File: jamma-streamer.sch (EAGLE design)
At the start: 73 parts, among them IC1 LM7805, J1 Audio line out, J2 ICSP, J3 796136-1, J4 DM3AT-SF-PEJM5, J6 292304-1, T1 TY-145P, T2 TY-145P, U1 CD74HC165MD16-M, U10 LM358DTD8-M, U2 ATMEGA328PB-AUR, U3 74HC4050D, U4 TLV757X / LP298X, U5 CD74HC165MD16-M, U6 CD74HC165MD16-M, U7 FT232RL, U8 DS3231SNT&R21-0042B_16-M, U9 NDT2955SOT-223-M, Y1 16MHz

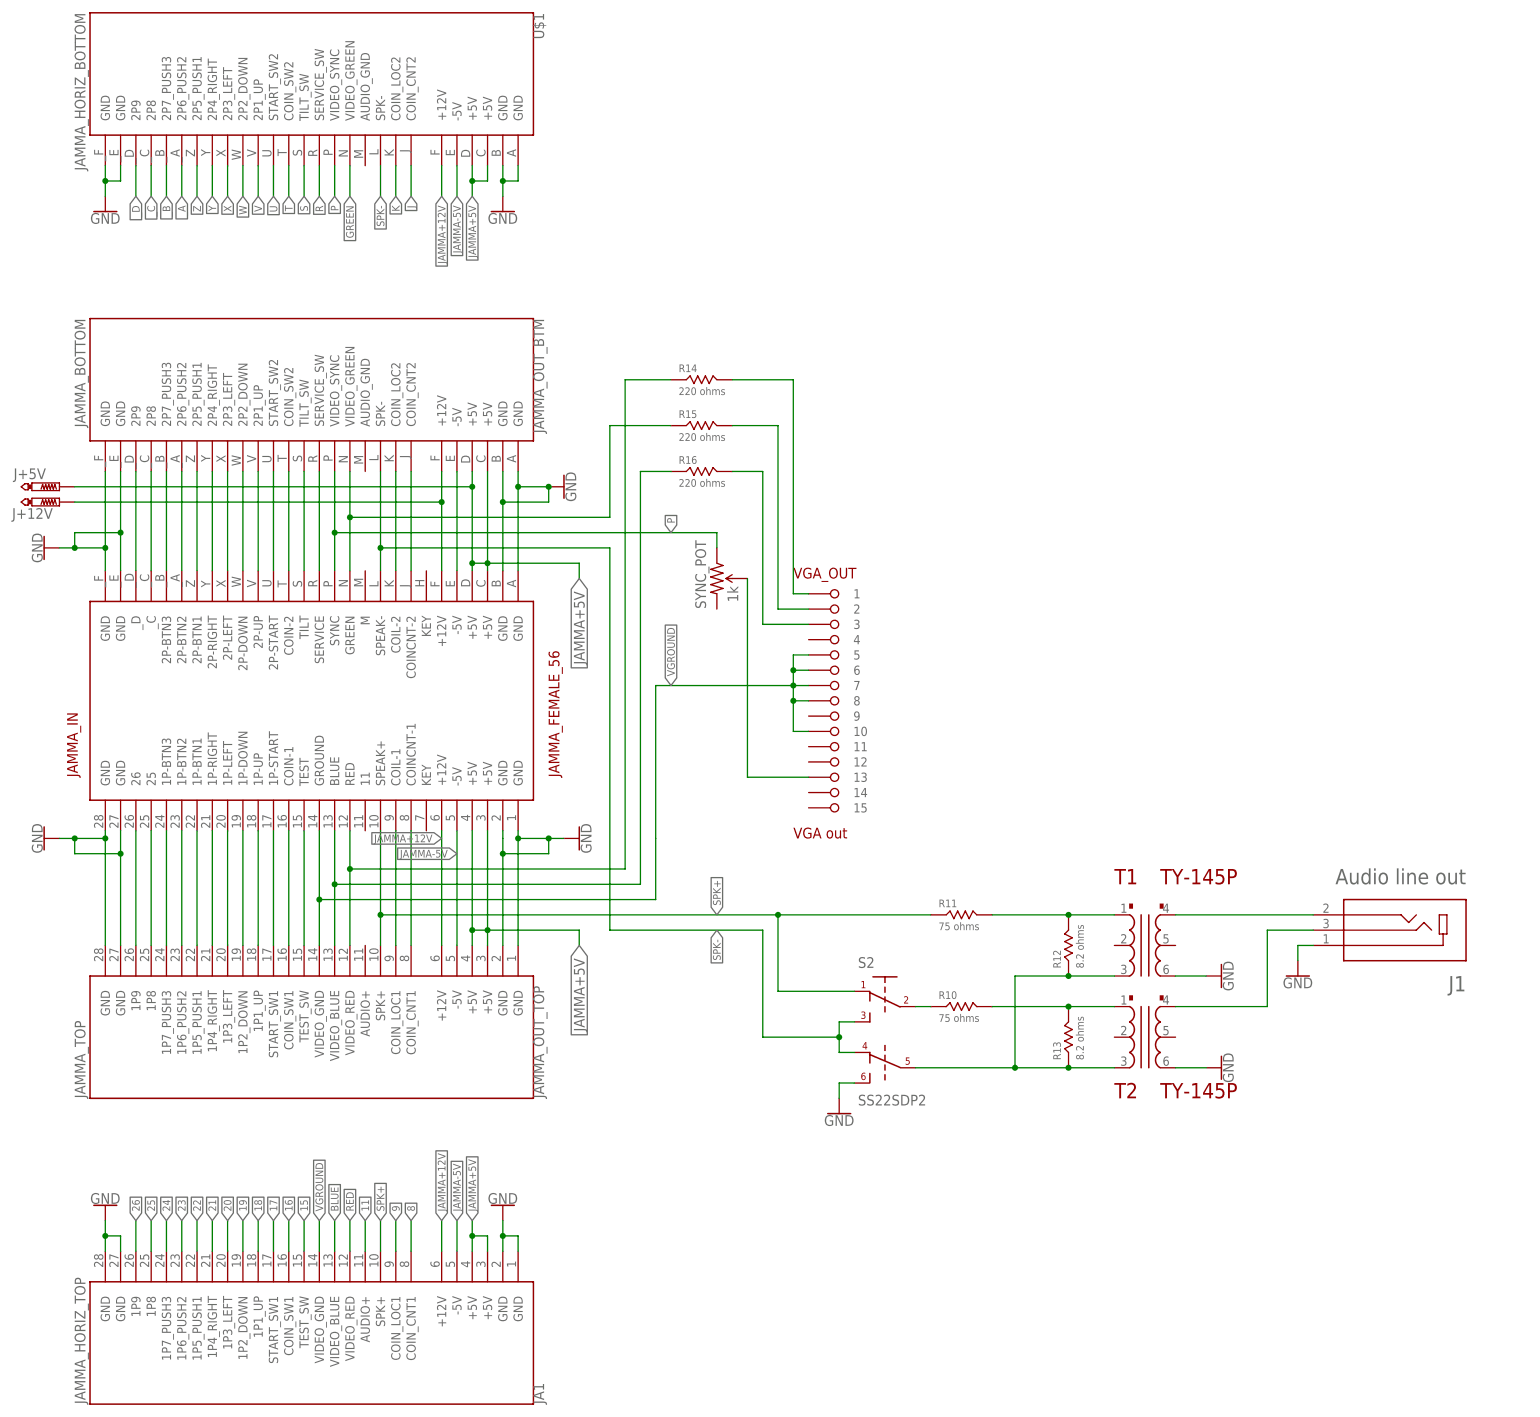
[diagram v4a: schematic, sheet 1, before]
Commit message: DRC Sparkfun ok
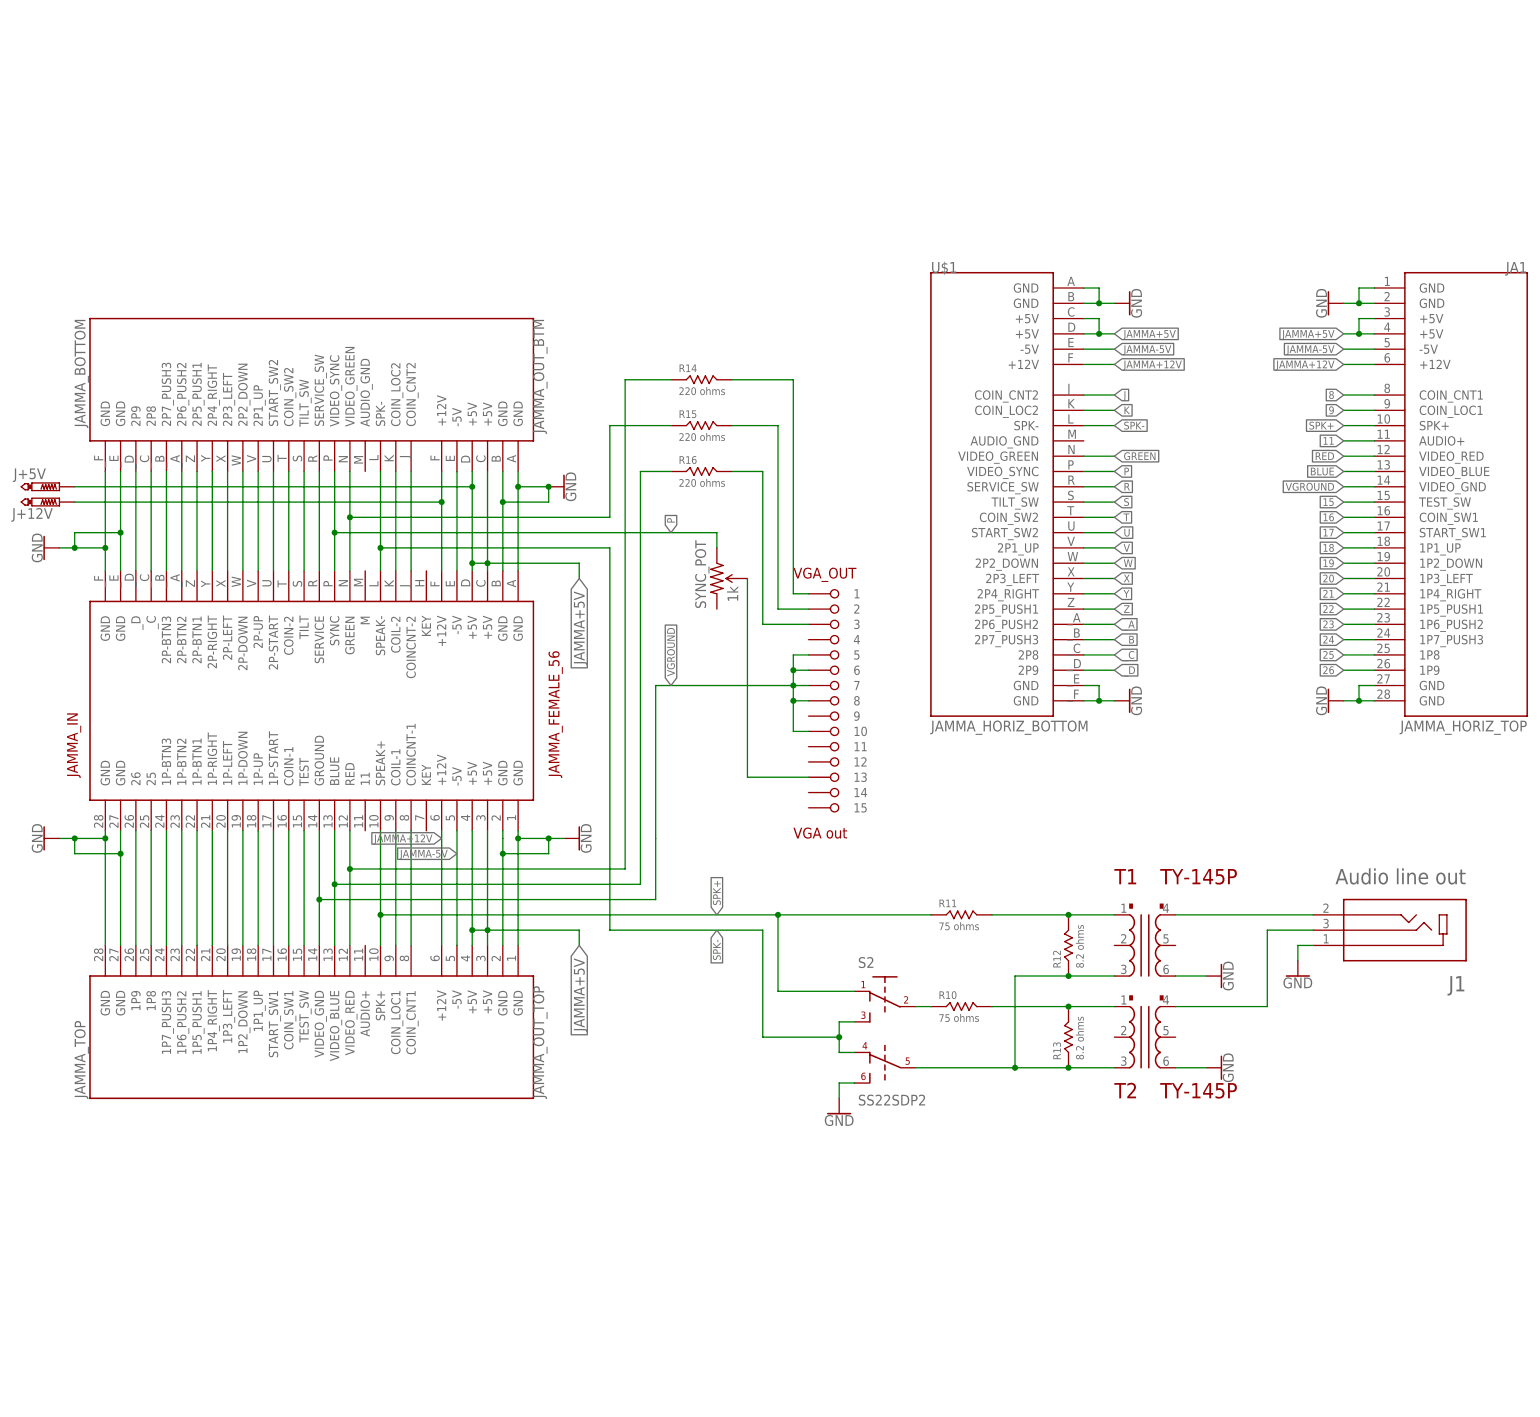
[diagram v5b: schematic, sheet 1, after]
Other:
- moved on the sheet: JA1, U$1
